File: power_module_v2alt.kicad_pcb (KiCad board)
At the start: 4 copper layers, 100 x 85 mm, 77 parts, among them J1_BMS1 I2C+ALERT, J1_INPUT1 USB_C_16P, Q1_BMS1 AON7544, Q1_BUCKBOOST1 AON7544, Q2_BMS1 AON7544, Q2_BUCKBOOST1 AON7544, Q3_BUCKBOOST1 AON7544, Q4_BUCKBOOST1 AON7544, SW1_BMS1 Kill Switch, U1_BMS1 BQ7692003PWR, U1_BUCKBOOST1 LM5176PWP, U1_CHARGER1 IP2326, U1_INPUT1 CH224K

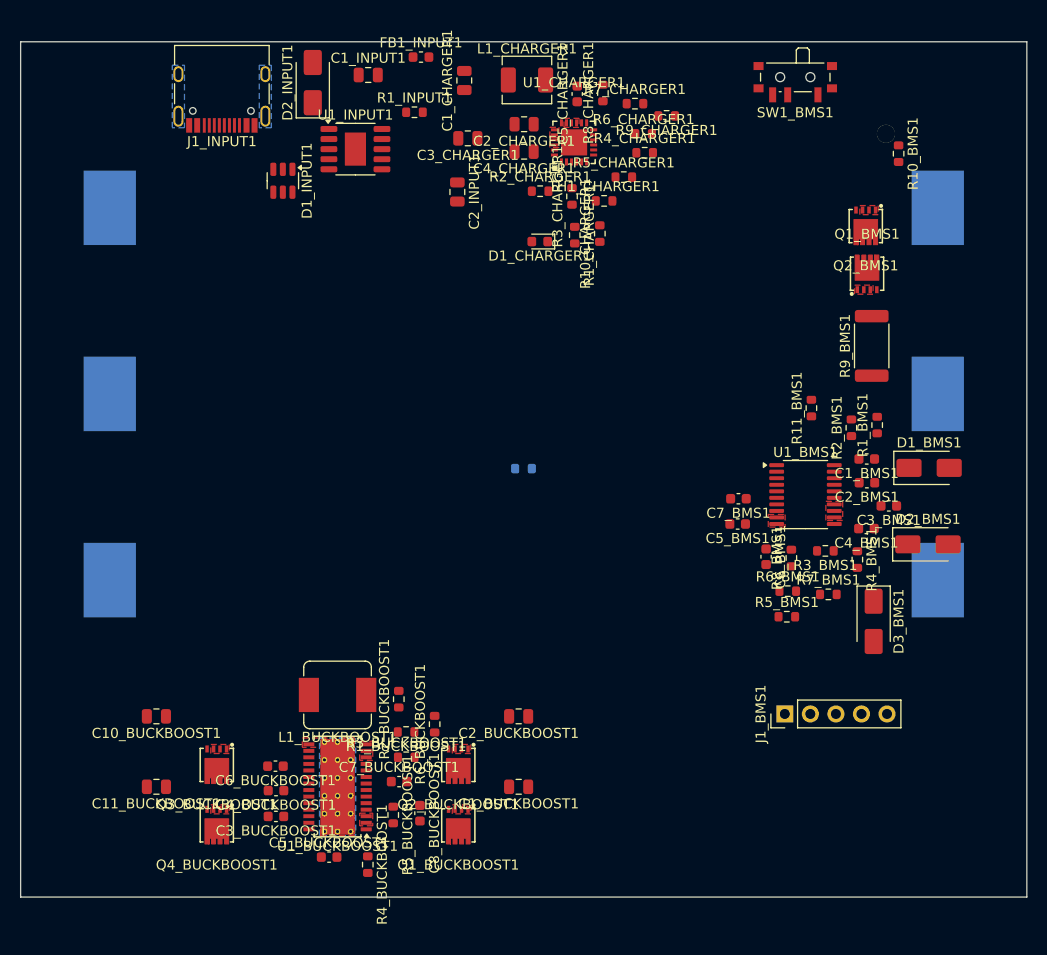
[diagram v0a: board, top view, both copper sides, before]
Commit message: Step 6+7 partial: freerouting + via_orphan_pads pass (26 unrouted remaining)
Full-board autoroute: 405 tracks, 23 vias, 78 unrouted from Freerouting
pass 1 (down to 61 in the DRC output after zone-refill).  Layer order
per feedback_4layer_routing_order: F.Cu → B.Cu → In2.Cu (PWR) → In1.Cu
(GND-last).

via_orphan_pads pass:
- GND: 37 vias placed (7 already connected, 6 skipped for no clearance)
- BAT+: 9 vias placed (5 skipped for no clearance)
- Drops orphan vias adjacent to F.Cu/B.Cu SMD pads that couldn't reach
  the (type power) inner plane during freerouting.  Required because
  freerouting refuses to place landing vias on power-typed layers.

Post-refill DRC: 61 → 26 unconnected.  Remaining 26 across 15 nets:
  GND: 6, BAT+: 2, CELL2_TOP: 2, VBUS_RAW: 2, CELL1_TOP: 2, VBUS_9V: 2,
  VSS: 2, TS1: 1, BAT-: 1, VSYS: 1, LED_K: 1, LX_SW: 1, VC3: 1,
  REGOUT: 1, SW1: 1.  Categories:
  - BAT1 cell-sense wires (CELL1/2_TOP, BAT-, part of BAT+): cross-
    board from B.Cu holder pads to F.Cu BMS sense R's
  - Signal-level stragglers freerouting missed
  - Small pin-zone → plane gaps needing manual bridging

Note: an intermediate incremental autoroute attempt on the remaining
15 nets removed 245 existing tracks and only added 149, making GND
much worse (26 → 58 unconnected).  Reverted to the pre-incremental
state; will address the remaining 26 with route_pad_to_pad or hand
routing rather than another whole-net rewrite.

Co-Authored-By: Claude Opus 4.7 <noreply@anthropic.com>
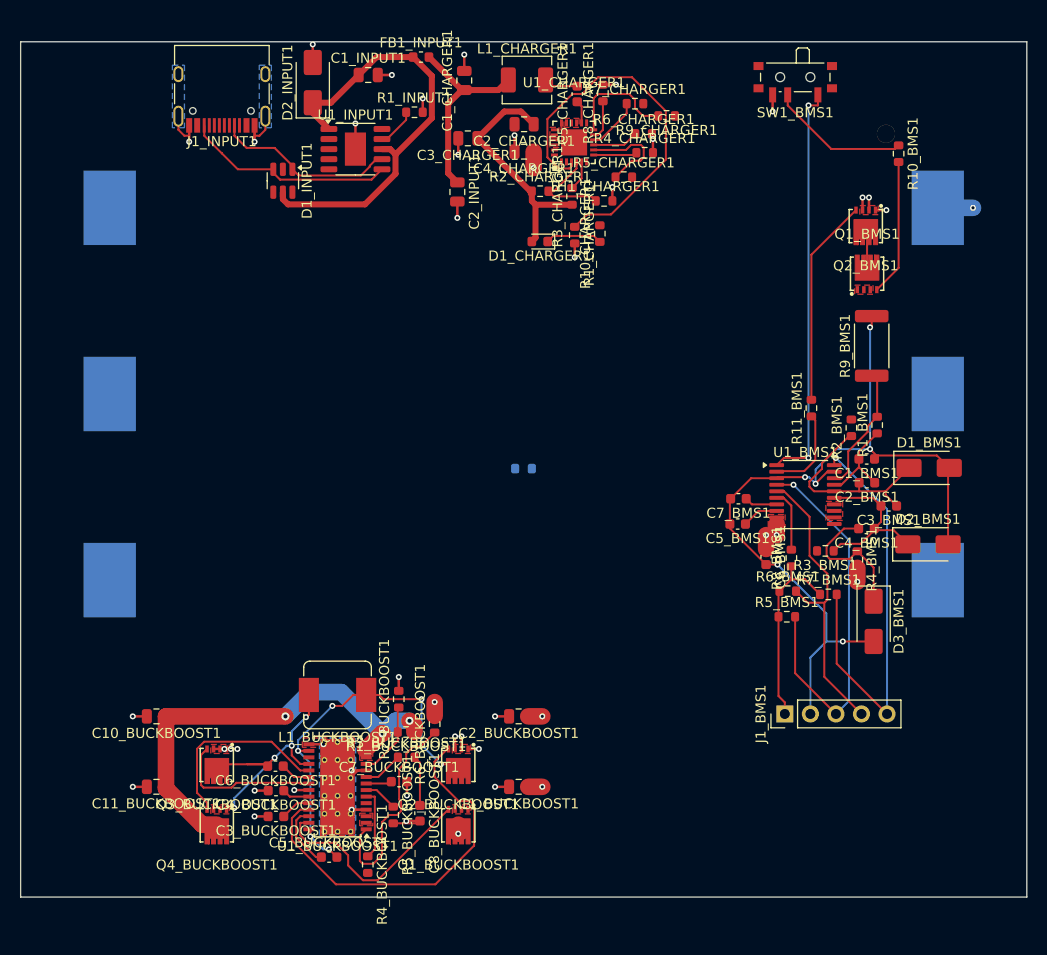
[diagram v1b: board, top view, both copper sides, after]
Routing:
- net VSS: track 0.00 -> 81.1 mm, vias 0 -> 6
- net GND: track 0.00 -> 69.6 mm, vias 0 -> 37
- net VOUT_12V: track 0.00 -> 44.8 mm, vias 0 -> 3
- net VBUS_RAW: track 0.00 -> 43.9 mm
- net ALERT: track 0.00 -> 42.3 mm, vias 0 -> 1
- net DSG_DRV: track 0.00 -> 40.5 mm, vias 0 -> 2
- net VSET: track 0.00 -> 38.8 mm
- net SW1: track 0.00 -> 38.7 mm, vias 0 -> 6
- net SDA: track 0.00 -> 38.6 mm, vias 0 -> 1
- net LDRV1: track 0.00 -> 38.3 mm
- net SCL: track 0.00 -> 29.6 mm
- net SW2: track 0.00 -> 26.7 mm, vias 0 -> 4
- net VSYS: track 0.00 -> 23.7 mm
- net REGOUT: track 0.00 -> 22.6 mm
- net HDRV1: track 0.00 -> 22.2 mm
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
